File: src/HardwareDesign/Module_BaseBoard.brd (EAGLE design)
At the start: 195.6 x 114 mm, 84 parts, among them IC1 RT9742GGJ, IC2 AP22653W6, IC3 74LVC1G07, IC4 RT9742NGV, IC5 AP3441SHE-7B, J1 692121030100, J2 692121030100, J3 FH12-22S-0.5SVA, J4 FH12-22S-0.5SVA, SW1 1825027-8, X1 CON-VG_MAB642, X2 CRYSTAL, X3 CON-VG_MAB642

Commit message: finish PCB desing
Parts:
- C1, C10, C11, C12, C13, C2, C20, C3, C4, C5, C9: device ds_passive:0402 -> ds_passive:C0402
- C14, C15, C16, C17, C18, C19, C6, C7: device ds_passive:0805 -> ds_passive:C0805
- moved R7 3.64 mm to (158.6, 79.6)
- moved R6 3.64 mm to (158.6, 78.4)
- moved J3 2.87 mm to (95.4, 28.6)
- moved TP-5VP 2.84 mm to (160.4, 81.3)
- moved TP-BTN 1.36 mm to (148.1, 90.2)
- moved C17 0.68 mm to (158.0, -7.78)
- moved C14 0.68 mm to (158.0, -3.31)
- moved C16 0.68 mm to (158.0, -5.56)
- moved C15 0.67 mm to (158.0, -1.17)
- renumbered X1 to MODULE_AIO, X3 to MODULE_DIO
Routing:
- net SCL0: track 0.00 -> 142.6 mm, vias 0 -> 8
- net SDA0: track 0.00 -> 134.9 mm, vias 0 -> 8
- net SDA1: track 2.44 -> 120.4 mm, vias 0 -> 1
- net SCL1: track 2.47 -> 114.8 mm, vias 0 -> 1
- net CAM_GPIO1: track 0.00 -> 109.9 mm, vias 0 -> 6
- net CAM_GPIO0: track 0.00 -> 94.1 mm, vias 0 -> 2
- net GND: track 582.8 -> 665.8 mm, vias 60 -> 178
- net DPHY0_D3_P: track 0.00 -> 55.1 mm, vias 0 -> 2
- net DPHY0_D3_N: track 0.00 -> 54.5 mm, vias 0 -> 2
- net DPHY0_D2_P: track 0.00 -> 53.5 mm, vias 0 -> 2
- net DPHY0_D2_N: track 0.00 -> 52.6 mm, vias 0 -> 2
- net DPHY0_C_P: track 0.00 -> 51.6 mm, vias 0 -> 2
- net DPHY0_C_N: track 0.00 -> 51.2 mm, vias 0 -> 2
- net DPHY0_D1_P: track 0.00 -> 50.6 mm, vias 0 -> 2
- net DPHY0_D1_N: track 0.00 -> 50.3 mm, vias 0 -> 2
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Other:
- outline, holes or cut-outs redrawn

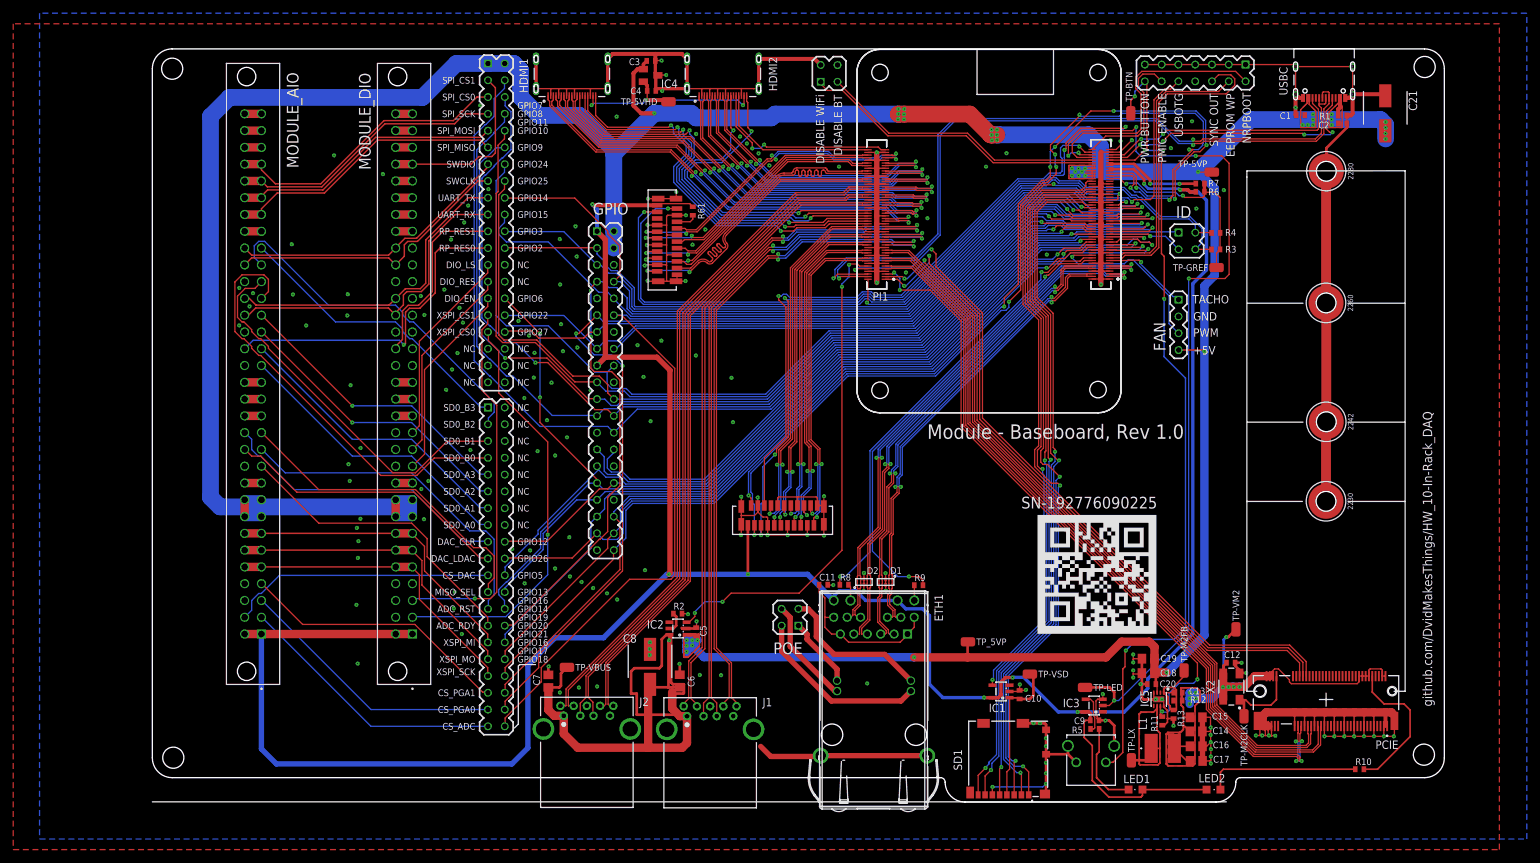
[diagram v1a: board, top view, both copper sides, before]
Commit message: add diffpaircheck
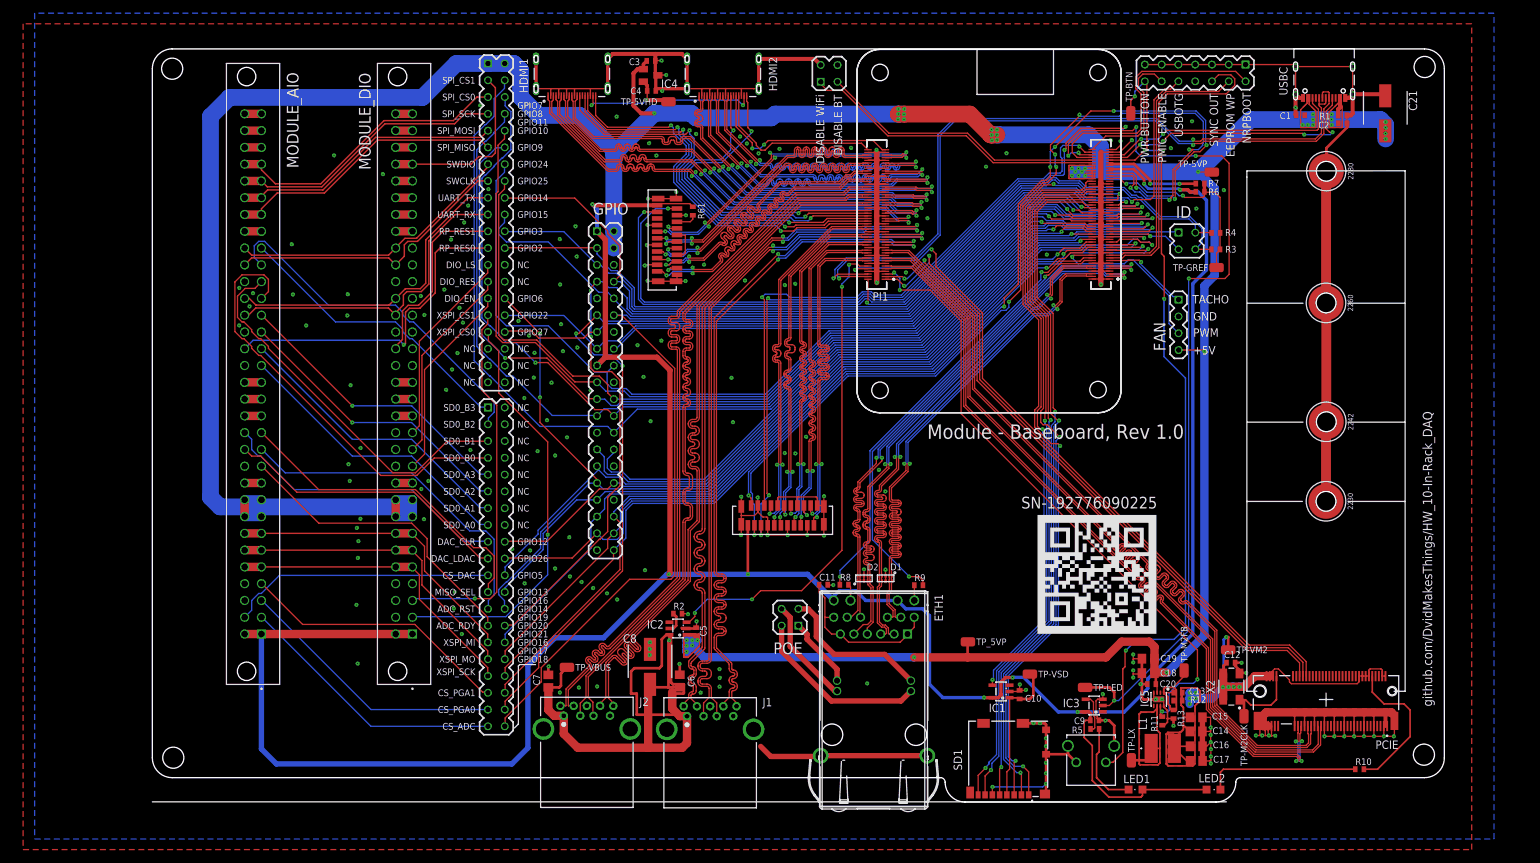
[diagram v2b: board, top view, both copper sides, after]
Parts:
- moved TP-VM2 3.32 mm to (162.8, 9.04), turned to 0 degrees
- moved D1 0.55 mm to (111.0, 19.9)
- moved D2 0.55 mm to (107.7, 19.9)
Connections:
- net DPHY0_C_N renamed DPHY0_DSIC_N
- net DPHY0_C_P renamed DPHY0_DSIC_P
- net DPHY0_D0_N renamed DPHY0_DSID0_N
- net DPHY0_D0_P renamed DPHY0_DSID0_P
- net DPHY0_D1_N renamed DPHY0_DSID1_N
- net DPHY0_D1_P renamed DPHY0_DSID1_P
- net DPHY0_D2_N renamed DPHY0_DSID2_N
- net DPHY0_D2_P renamed DPHY0_DSID2_P
- net DPHY0_D3_N renamed DPHY0_DSID3_N
- net DPHY0_D3_P renamed DPHY0_DSID3_P
- net DPHY1_C_N renamed DPHY1_DSIC_N
- net DPHY1_C_P renamed DPHY1_DSIC_P
- net DPHY1_D0_N renamed DPHY1_DSID0_N
- net DPHY1_D0_P renamed DPHY1_DSID0_P
- net DPHY1_D1_N renamed DPHY1_DSID1_N
- net DPHY1_D1_P renamed DPHY1_DSID1_P
- net DPHY1_D2_N renamed DPHY1_DSID2_N
- net DPHY1_D2_P renamed DPHY1_DSID2_P
- net DPHY1_D3_N renamed DPHY1_DSID3_N
- net DPHY1_D3_P renamed DPHY1_DSID3_P
- net HDMI0_CK_N renamed HDMI0_TDMSCK_N
- net HDMI0_CK_P renamed HDMI0_TDMSCK_P
- net HDMI0_D0_N renamed HDMI0_TDMS0_N
- net HDMI0_D0_P renamed HDMI0_TDMS0_P
- net HDMI0_D1_N renamed HDMI0_TDMS1_N
- net HDMI0_D1_P renamed HDMI0_TDMS1_P
- net HDMI0_D2_N renamed HDMI0_TDMS2_N
- net HDMI0_D2_P renamed HDMI0_TDMS2_P
- net HDMI1_CK_N renamed HDMI1_TDMSCK_N
- net HDMI1_CK_P renamed HDMI1_TDMSCK_P
- net HDMI1_D0_N renamed HDMI1_TDMS0_N
- net HDMI1_D0_P renamed HDMI1_TDMS0_P
- net HDMI1_D1_N renamed HDMI1_TDMS1_N
- net HDMI1_D1_P renamed HDMI1_TDMS1_P
- net HDMI1_D2_N renamed HDMI1_TDMS2_N
- net HDMI1_D2_P renamed HDMI1_TDMS2_P
- net TRD0_N renamed ETH_TX1_N
- net TRD0_P renamed ETH_TX1_P
- net TRD1_N renamed ETH_TX2_N
- net TRD1_P renamed ETH_TX2_P
- net TRD2_N renamed ETH_TX3_N
- net TRD2_P renamed ETH_TX3_P
- net TRD3_N renamed ETH_TX4_N
- net TRD3_P renamed ETH_TX4_P
- net USB2_N renamed USB_DP_N
- net USB2_P renamed USB_DP_P
- net USB3-0-D_N renamed USB3A_DP_N
- net USB3-0-D_P renamed USB3A_DP_P
- net USB3-0-RX_N renamed USB3A_SSRX_N
- net USB3-0-RX_P renamed USB3A_SSRX_P
- net USB3-0-TX_N renamed USB3A_SSTX_N
- net USB3-0-TX_P renamed USB3A_SSTX_P
- net USB3-1-D_N renamed USB3B_DP_N
- net USB3-1-D_P renamed USB3B_DP_P
- net USB3-1-RX_N renamed USB3B_SSRX_N
- net USB3-1-RX_P renamed USB3B_SSRX_P
- net USB3-1-TX_N renamed USB3B_SSTX_N
- net USB3-1-TX_P renamed USB3B_SSTX_P
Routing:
- net ETH_TX4_P: track 69.1 -> 85.6 mm
- net ETH_TX4_N: track 69.6 -> 85.6 mm
- net DPHY1_DSID2_N: track 34.2 -> 48.8 mm, vias 0 -> 2
- net GND: track 665.8 -> 651.2 mm, vias 178 -> 186
- net USB3B_SSRX_N: track 98.7 -> 113.1 mm
- net USB3B_SSRX_P: track 99.3 -> 113.1 mm
- net DPHY1_DSIC_P: track 35.1 -> 48.6 mm, vias 0 -> 2
- net ETH_TX3_N: track 74.0 -> 85.8 mm
- net ETH_TX3_P: track 74.5 -> 85.8 mm
- net USB3B_DP_P: track 102.2 -> 112.7 mm
- net USB3B_SSTX_N: track 103.6 -> 113.7 mm
- net USB3B_DP_N: track 102.8 -> 112.7 mm
- net USB3B_SSTX_P: track 104.2 -> 113.7 mm
- net USB3A_SSRX_N: track 100.8 -> 110.0 mm
- net USB3A_SSRX_P: track 101.4 -> 110.0 mm
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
